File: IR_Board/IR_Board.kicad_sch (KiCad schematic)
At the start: 64 parts, among them J1 Conn_02x08_Top_Bottom, Q1 FDG6335N, Q10 FDG6335N, Q11 FDG6335N, Q12 FDG6335N, Q13 FDG6335N, Q14 FDG6335N, Q2 FDG6335N, Q3 FDG6335N, Q4 FDG6335N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

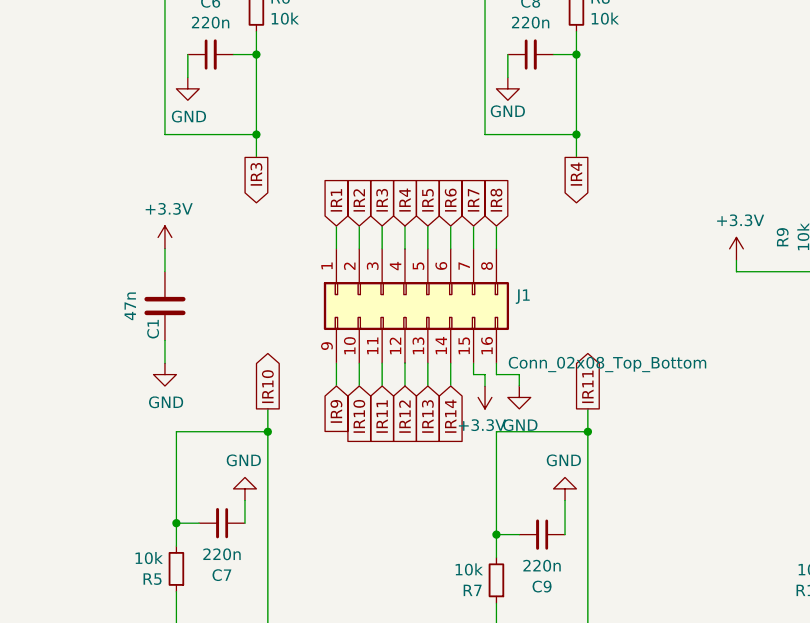
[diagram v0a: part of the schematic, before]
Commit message: Started drawing traces [IR BOARD]
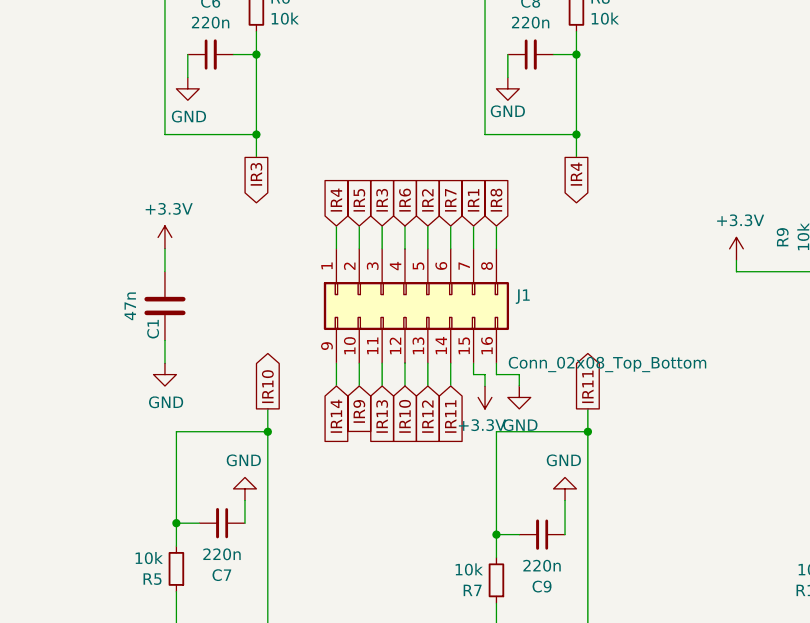
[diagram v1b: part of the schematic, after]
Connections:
- net IR1: now also J1.7 (Pin_7); no longer J1.1 (Pin_1)
- net IR10: now also J1.12 (Pin_12); no longer J1.10 (Pin_10)
- net IR11: now also J1.14 (Pin_14); no longer J1.11 (Pin_11)
- net IR12: now also J1.13 (Pin_13); no longer J1.12 (Pin_12)
- net IR13: now also J1.11 (Pin_11); no longer J1.13 (Pin_13)
- net IR14: now also J1.9 (Pin_9); no longer J1.14 (Pin_14)
- net IR2: now also J1.5 (Pin_5); no longer J1.2 (Pin_2)
- net IR4: now also J1.1 (Pin_1); no longer J1.4 (Pin_4)
- net IR5: now also J1.2 (Pin_2); no longer J1.5 (Pin_5)
- net IR6: now also J1.4 (Pin_4); no longer J1.6 (Pin_6)
- net IR7: now also J1.6 (Pin_6); no longer J1.7 (Pin_7)
- net IR9: now also J1.10 (Pin_10); no longer J1.9 (Pin_9)

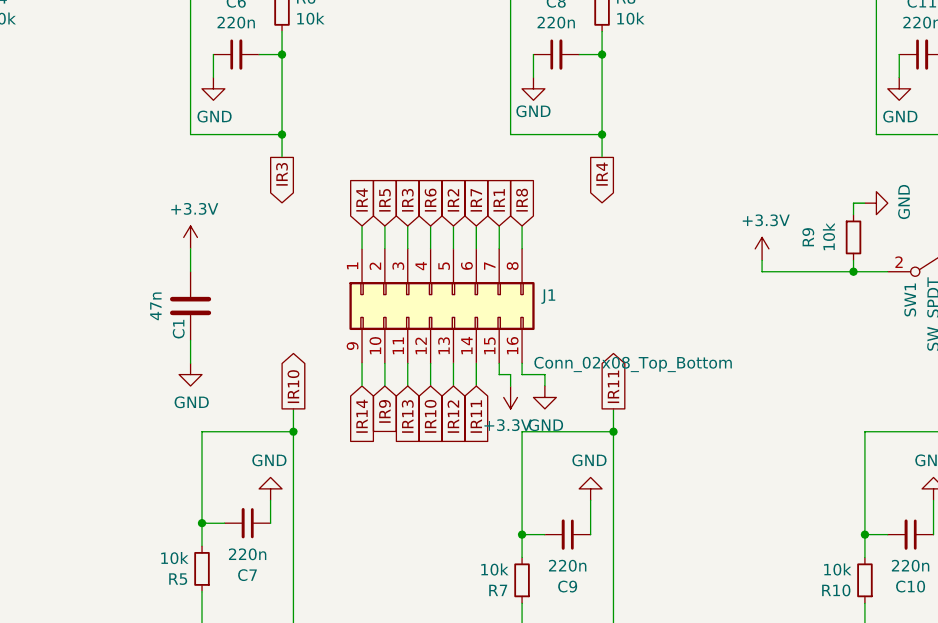
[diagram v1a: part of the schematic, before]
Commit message: Continued drawing traces [IR BOARD]
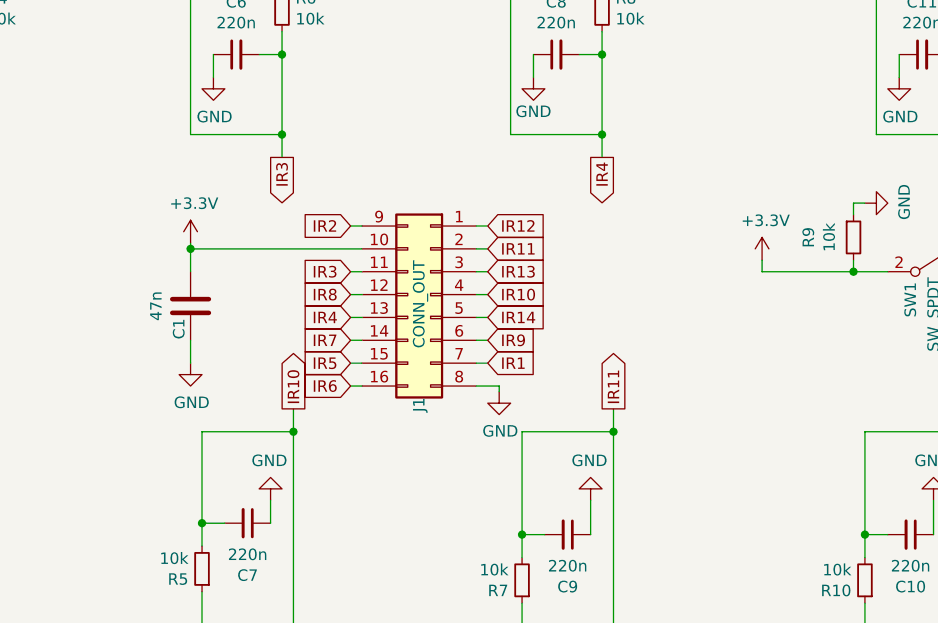
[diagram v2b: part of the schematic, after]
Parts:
- C1: footprint Capacitor_SMD:C_0603_1608Metric -> Capacitor_SMD:C_0201_0603Metric
- C10, C11, C12, C13, C14, C15, C2, C3, C4, C5, C6, C7, C8, C9: footprint Capacitor_SMD:C_0603_1608Metric -> Capacitor_SMD:C_0805_2012Metric_Pad1.18x1.45mm_HandSolder
- J1: value Conn_02x08_Top_Bottom -> CONN_OUT
- R1, R10, R11, R12, R13, R14, R15, R16, R17, R2, R3, R4, R5, R6, R7, R8, R9: footprint Resistor_SMD:R_0603_1608Metric -> Resistor_SMD:R_0805_2012Metric_Pad1.20x1.40mm_HandSolder
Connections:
- net +3V3: now also J1.10 (Pin_10); no longer J1.15 (Pin_15)
- net GND: now also J1.8 (Pin_8); no longer J1.16 (Pin_16)
- net IR10: now also J1.4 (Pin_4); no longer J1.12 (Pin_12)
- net IR11: now also J1.2 (Pin_2); no longer J1.14 (Pin_14)
- net IR12: now also J1.1 (Pin_1); no longer J1.13 (Pin_13)
- net IR13: now also J1.3 (Pin_3); no longer J1.11 (Pin_11)
- net IR14: now also J1.5 (Pin_5); no longer J1.9 (Pin_9)
- net IR2: now also J1.9 (Pin_9); no longer J1.5 (Pin_5)
- net IR3: now also J1.11 (Pin_11); no longer J1.3 (Pin_3)
- net IR4: now also J1.13 (Pin_13); no longer J1.1 (Pin_1)
- net IR5: now also J1.15 (Pin_15); no longer J1.2 (Pin_2)
- net IR6: now also J1.16 (Pin_16); no longer J1.4 (Pin_4)
- net IR7: now also J1.14 (Pin_14); no longer J1.6 (Pin_6)
- net IR8: now also J1.12 (Pin_12); no longer J1.8 (Pin_8)
- net IR9: now also J1.6 (Pin_6); no longer J1.10 (Pin_10)
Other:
- moved on the sheet: J1
